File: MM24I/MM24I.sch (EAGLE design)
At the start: 21 parts, among them IC1 SN74LVC2G17DBVR, IC2 SN74LVC14APWR, U1 SN74LVCH16374ADGGR, U2 SN74LVCH16374ADGGR, U3 CY14B104M, U4 SN74AHCT16373DGGR, X1 FH21-18S-1DSA, X2 FH21-18S-1DSA, X3 FH21-18S-1DSA, X4 FH21-18S-1DSA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

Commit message: Redesigned memory expansion to fit on a single flip chip, consolidated component libraries, etc.
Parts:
- removed X5: FH21-18S-1DSA, con-hirose:FH21-18S-1DSA
- added C4: 0.1 UF, rcl:C-USC0805
- added R5: 10k, rcl:R-US_R1206
- added U$1: SINGLE, dec-con:SINGLE
- added U5: TLV803SDBZ, MM24I:TLV803SDBZ
- C1: value 470UF -> 100UF; device AVX_By_element14_Batch_1:NOSE477M004R0100 -> MM24I:NOJD107M010RWJ
- C2: device MM24I:C0603C474K8PACTU -> rcl:C-USC0805
- X1, X2, X3, X4: value FH21-18S-1DSA -> FH12-18S-0.5SV(55); device con-hirose:FH21-18S-1DSA -> MM24I:FH12-18S-0.5SV(55)
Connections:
- net N$1 renamed VCAP
- new net !POWER-OK: R5.2, U3.!CE, U5.!RESET
- new net N$1: C4.2, U5.VDD
- net +5V: now also C4.1
- net GND: now also U$1C2.1, U$1F2.1, U$1J2.1, U$1L2.1, U$1N2.1, U$1R2.1, U$1U2.1, U5.GND; no longer U3.!CE, X5.10, X5.12, X5.14, X5.17, X5.3, X5.6, X5.8
- net MCS-MEM-08-H: now also U$1D2.1; no longer X5.4
- net MCS-MEM-09-H: now also U$1E2.1; no longer X5.5
- net MCS-MEM-10-H: now also U$1H2.1; no longer X5.7
- net MCS-MEM-11-H: now also U$1K2.1; no longer X5.9
- net MCT-MEM-DONE-L: now also U$1S2.1; no longer X5.15
- net MCT-STROBE-L: now also U$1P2.1; no longer X5.13
- net MXB-MEM-TP3-H: now also U$1V2.1; no longer X5.18
- net MXB-START-MEMORY-H: now also U$1M2.1; no longer X5.11
- net VCC: now also R5.1

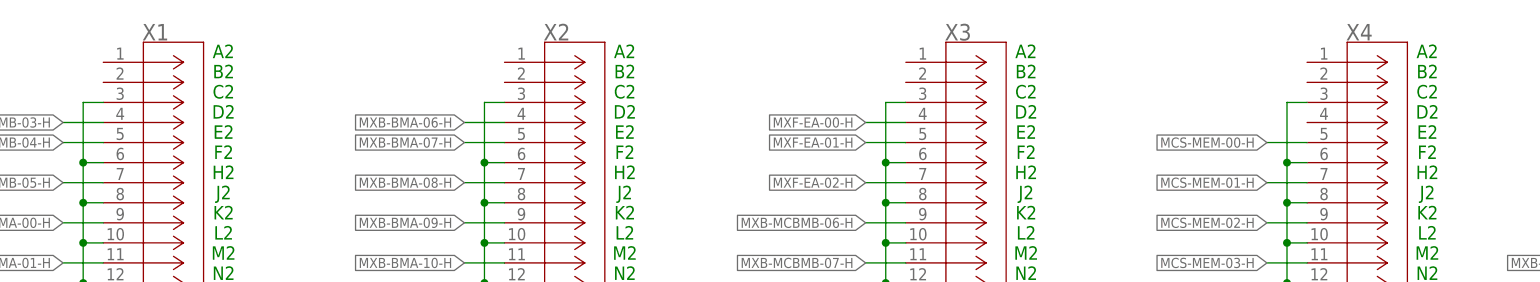
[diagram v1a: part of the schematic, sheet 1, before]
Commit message: Fix typo in , change FFC reference designators to match backplane slot names on MM24I
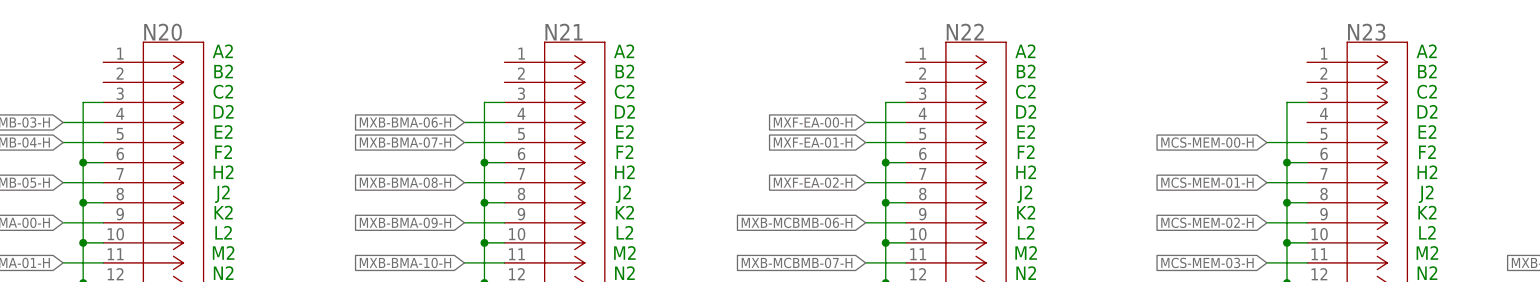
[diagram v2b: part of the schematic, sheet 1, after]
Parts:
- renumbered X1 to N20, X2 to N21, X3 to N22, X4 to N23

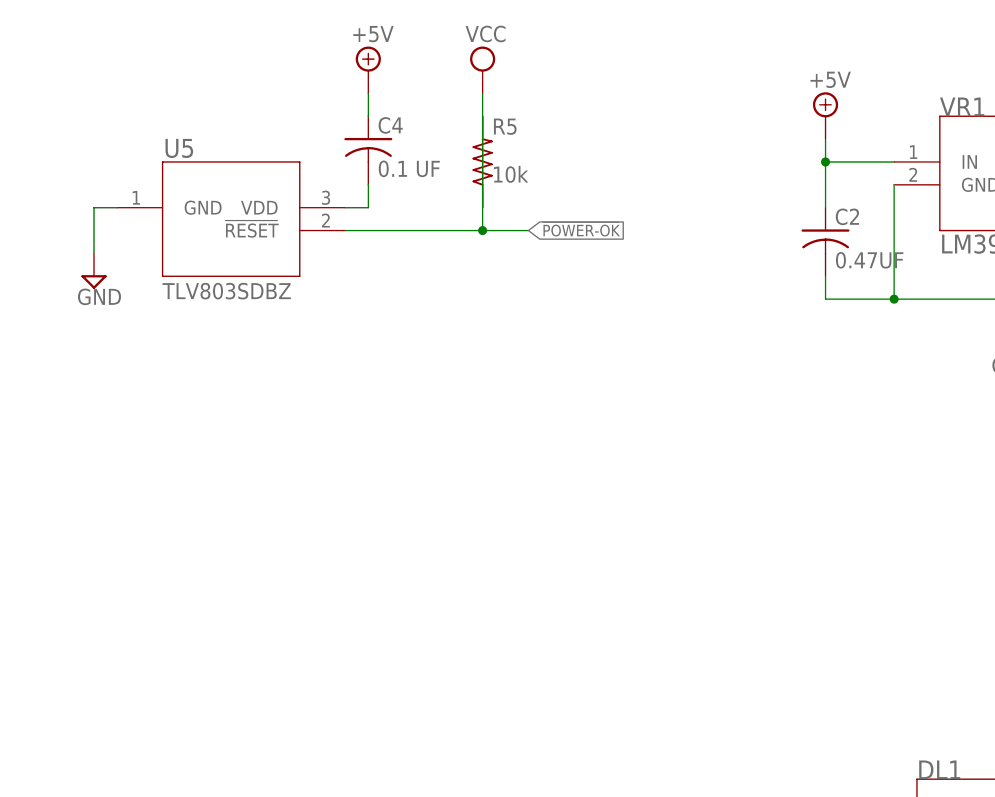
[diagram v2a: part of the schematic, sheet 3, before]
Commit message: Add bypass capacitors to schematic
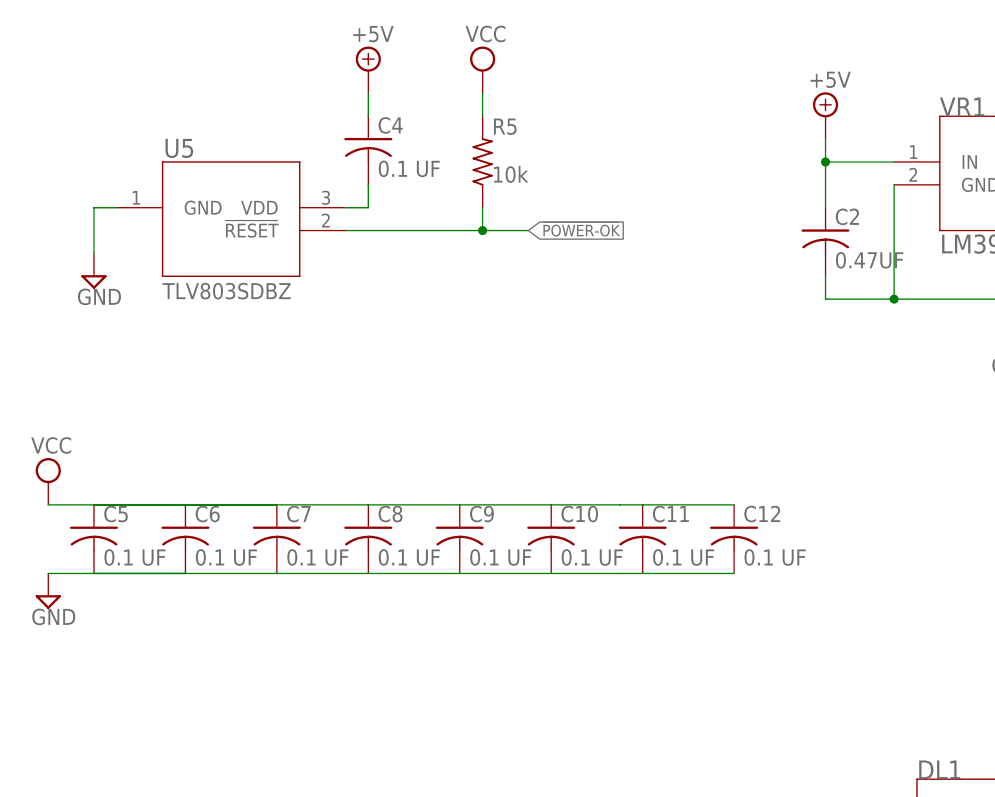
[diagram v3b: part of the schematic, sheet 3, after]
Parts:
- added C10, C11, C12, C5, C6, C7, C8, C9: 0.1 UF, rcl:C-USC0805
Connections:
- net !POWER-OK: now also R5.1; no longer R5.2
- net GND: now also C10.2, C11.2, C12.2, C5.2, C6.2, C7.2, C8.2, C9.2
- net VCC: now also C10.1, C11.1, C12.1, C5.1, C6.1, C7.1, C8.1, C9.1, R5.2; no longer R5.1
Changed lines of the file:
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@@
 <part name="SUPPLY28" library="supply2" library_urn="urn:adsk.eagle:library:372" deviceset="+5V" device=""/>
 <part name="C4" library="rcl" library_urn="urn:adsk.eagle:library:334" deviceset="C-US" device="C0805" package3d_urn="urn:adsk.eagle:package:23617/2" value="0.1 UF"/>
+<part name="SUPPLY29" library="supply2" library_urn="urn:adsk.eagle:library:372" deviceset="VCC" device=""/>
+<part name="SUPPLY30" library="supply2" library_urn="urn:adsk.eagle:library:372" deviceset="GND" device=""/>
+<part name="C5" library="rcl" library_urn="urn:adsk.eagle:library:334" deviceset="C-US" device="C0805" package3d_urn="urn:adsk.eagle:package:23617/2" value="0.1 UF"/>
+<part name="C6" library="rcl" library_urn="urn:adsk.eagle:library:334" deviceset="C-US" device="C0805" package3d_urn="urn:adsk.eagle:package:23617/2" value="0.1 UF"/>
+<part name="C7" library="rcl" library_urn="urn:adsk.eagle:library:334" deviceset="C-US" device="C0805" package3d_urn="urn:adsk.eagle:package:23617/2" value="0.1 UF"/>
+<part name="C8" library="rcl" library_urn="urn:adsk.eagle:library:334" deviceset="C-US" device="C0805" package3d_urn="urn:adsk.eagle:package:23617/2" value="0.1 UF"/>
+<part name="C9" library="rcl" library_urn="urn:adsk.eagle:library:334" deviceset="C-US" device="C0805" package3d_urn="urn:adsk.eagle:package:23617/2" value="0.1 UF"/>
+<part name="C10" library="rcl" library_urn="urn:adsk.eagle:library:334" deviceset="C-US" device="C0805" package3d_urn="urn:adsk.eagle:package:23617/2" value="0.1 UF"/>
+<part name="C11" library="rcl" library_urn="urn:adsk.eagle:library:334" deviceset="C-US" device="C0805" package3d_urn="urn:adsk.eagle:package:23617/2" value="0.1 UF"/>
+<part name="C12" library="rcl" library_urn="urn:adsk.eagle:library:334" deviceset="C-US" device="C0805" package3d_urn="urn:adsk.eagle:package:23617/2" value="0.1 UF"/>
 </parts>
 <sheets>
@@
 <sheet>
 <plain>
-<text x="210.82" y="121.92" size="1.778" layer="97">MEM Register</text>
+<text x="203.2" y="53.34" size="1.778" layer="97">MEM Register</text>
 <text x="45.72" y="129.54" size="1.778" layer="97">MB Buffer</text>
 <text x="45.72" y="53.34" size="1.778" layer="97">MA Buffer</text>
@@
 <attribute name="VALUE" x="74.676" y="163.449" size="1.778" layer="96"/>
 </instance>
+<instance part="SUPPLY29" gate="G$1" x="38.1" y="129.54" smashed="yes">
+<attribute name="VALUE" x="36.195" y="132.715" size="1.778" layer="96"/>
+</instance>
+<instance part="SUPPLY30" gate="GND" x="38.1" y="116.84" smashed="yes">
+<attribute name="VALUE" x="36.195" y="113.665" size="1.778" layer="96"/>
+</instance>
+<instance part="C5" gate="G$1" x="43.18" y="124.46" smashed="yes">
+<attribute name="NAME" x="44.196" y="125.095" size="1.778" layer="95"/>
+<attribute name="VALUE" x="44.196" y="120.269" size="1.778" layer="96"/>
+</instance>
+<instance part="C6" gate="G$1" x="53.34" y="124.46" smashed="yes">
+<attribute name="NAME" x="54.356" y="125.095" size="1.778" layer="95"/>
+<attribute name="VALUE" x="54.356" y="120.269" size="1.778" layer="96"/>
+</instance>
+<instance part="C7" gate="G$1" x="63.5" y="124.46" smashed="yes">
+<attribute name="NAME" x="64.516" y="125.095" size="1.778" layer="95"/>
+<attribute name="VALUE" x="64.516" y="120.269" size="1.778" layer="96"/>
+</instance>
+<instance part="C8" gate="G$1" x="73.66" y="124.46" smashed="yes">
+<attribute name="NAME" x="74.676" y="125.095" size="1.778" layer="95"/>
+<attribute name="VALUE" x="74.676" y="120.269" size="1.778" layer="96"/>
+</instance>
+<instance part="C9" gate="G$1" x="83.82" y="124.46" smashed="yes">
+<attribute name="NAME" x="84.836" y="125.095" size="1.778" layer="95"/>
+<attribute name="VALUE" x="84.836" y="120.269" size="1.778" layer="96"/>
+</instance>
+<instance part="C10" gate="G$1" x="93.98" y="124.46" smashed="yes">
+<attribute name="NAME" x="94.996" y="125.095" size="1.778" layer="95"/>
+<attribute name="VALUE" x="94.996" y="120.269" size="1.778" layer="96"/>
+</instance>
+<instance part="C11" gate="G$1" x="104.14" y="124.46" smashed="yes">
+<attribute name="NAME" x="105.156" y="125.095" size="1.778" layer="95"/>
+<attribute name="VALUE" x="105.156" y="120.269" size="1.778" layer="96"/>
+</instance>
+<instance part="C12" gate="G$1" x="114.3" y="124.46" smashed="yes">
+<attribute name="NAME" x="115.316" y="125.095" size="1.778" layer="95"/>
+<attribute name="VALUE" x="115.316" y="120.269" size="1.778" layer="96"/>
+</instance>
 </instances>
 <busses>
@@
 <pinref part="U5" gate="A" pin="GND"/>
 </segment>
+<segment>
+<pinref part="SUPPLY30" gate="GND" pin="GND"/>
+<pinref part="C5" gate="G$1" pin="2"/>
+<wire x1="38.1" y1="119.38" x2="43.18" y2="119.38" width="0.1524" layer="91"/>
+<pinref part="C6" gate="G$1" pin="2"/>
+<wire x1="43.18" y1="119.38" x2="53.34" y2="119.38" width="0.1524" layer="91"/>
+<pinref part="C7" gate="G$1" pin="2"/>
+<wire x1="43.18" y1="119.38" x2="63.5" y2="119.38" width="0.1524" layer="91"/>
+<pinref part="C8" gate="G$1" pin="2"/>
+<wire x1="63.5" y1="119.38" x2="73.66" y2="119.38" width="0.1524" layer="91"/>
+<pinref part="C9" gate="G$1" pin="2"/>
+<wire x1="73.66" y1="119.38" x2="83.82" y2="119.38" width="0.1524" layer="91"/>
+<pinref part="C10" gate="G$1" pin="2"/>
+<wire x1="83.82" y1="119.38" x2="93.98" y2="119.38" width="0.1524" layer="91"/>
+<pinref part="C11" gate="G$1" pin="2"/>
+<wire x1="93.98" y1="119.38" x2="101.6" y2="119.38" width="0.1524" layer="91"/>
+<pinref part="C12" gate="G$1" pin="2"/>
+<wire x1="101.6" y1="119.38" x2="104.14" y2="119.38" width="0.1524" layer="91"/>
+<wire x1="104.14" y1="119.38" x2="114.3" y2="119.38" width="0.1524" layer="91"/>
+</segment>
 </net>
 <net name="VCC" class="1">
@@
 </segment>
 <segment>
+<pinref part="R5" gate="G$1" pin="2"/>
 <pinref part="SUPPLY27" gate="G$1" pin="VCC"/>
-<pinref part="R5" gate="G$1" pin="1"/>
-<wire x1="86.36" y1="172.72" x2="86.36" y2="160.02" width="0.1524" layer="91"/>
+<wire x1="86.36" y1="170.18" x2="86.36" y2="172.72" width="0.1524" layer="91"/>
+</segment>
+<segment>
+<pinref part="SUPPLY29" gate="G$1" pin="VCC"/>
+<pinref part="C5" gate="G$1" pin="1"/>
+<wire x1="38.1" y1="127" x2="43.18" y2="127" width="0.1524" layer="91"/>
+<pinref part="C6" gate="G$1" pin="1"/>
+<wire x1="43.18" y1="127" x2="53.34" y2="127" width="0.1524" layer="91"/>
+<pinref part="C7" gate="G$1" pin="1"/>
+<wire x1="43.18" y1="127" x2="63.5" y2="127" width="0.1524" layer="91"/>
+<pinref part="C8" gate="G$1" pin="1"/>
+<wire x1="43.18" y1="127" x2="73.66" y2="127" width="0.1524" layer="91"/>
+<pinref part="C9" gate="G$1" pin="1"/>
+<wire x1="73.66" y1="127" x2="83.82" y2="127" width="0.1524" layer="91"/>
+<pinref part="C10" gate="G$1" pin="1"/>
+<wire x1="83.82" y1="127" x2="93.98" y2="127" width="0.1524" layer="91"/>
+<pinref part="C11" gate="G$1" pin="1"/>
+<wire x1="93.98" y1="127" x2="101.6" y2="127" width="0.1524" layer="91"/>
+<pinref part="C12" gate="G$1" pin="1"/>
+<wire x1="101.6" y1="127" x2="104.14" y2="127" width="0.1524" layer="91"/>
+<wire x1="104.14" y1="127" x2="114.3" y2="127" width="0.1524" layer="91"/>
 </segment>
 </net>
@@
 <segment>
 <pinref part="U5" gate="A" pin="!RESET"/>
-<pinref part="R5" gate="G$1" pin="2"/>
 <wire x1="71.12" y1="157.48" x2="86.36" y2="157.48" width="0.1524" layer="91"/>
-<wire x1="86.36" y1="157.48" x2="86.36" y2="170.18" width="0.1524" layer="91"/>
+<label x="91.44" y="157.48" size="1.27" layer="95" xref="yes"/>
+<pinref part="R5" gate="G$1" pin="1"/>
 <wire x1="86.36" y1="157.48" x2="91.44" y2="157.48" width="0.1524" layer="91"/>
+<wire x1="86.36" y1="160.02" x2="86.36" y2="157.48" width="0.1524" layer="91"/>
 <junction x="86.36" y="157.48"/>
-<label x="91.44" y="157.48" size="1.27" layer="95" xref="yes"/>
-</segment>
-</net>
+</segment>
+</net>
